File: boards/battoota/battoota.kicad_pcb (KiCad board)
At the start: 2 copper layers, 122.6 x 88.9 mm, 23 parts

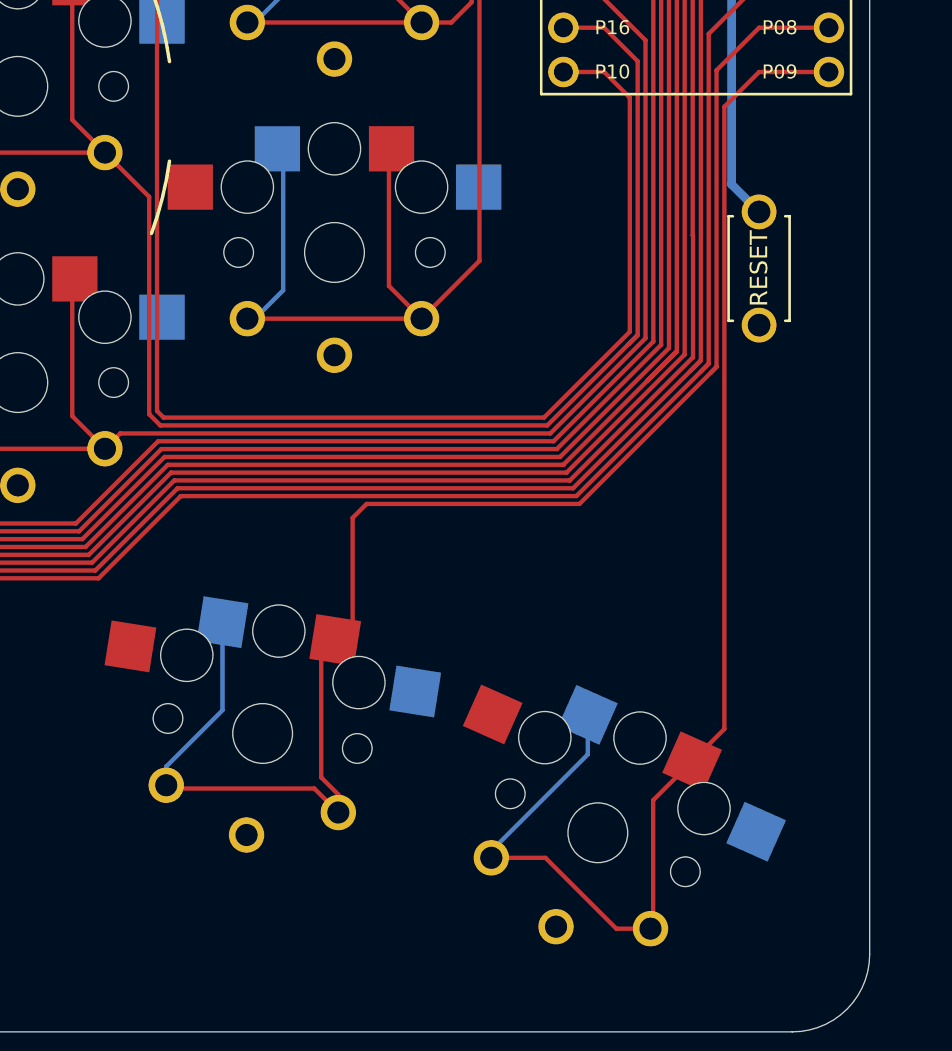
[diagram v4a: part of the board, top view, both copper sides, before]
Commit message: battoota thumb to original place
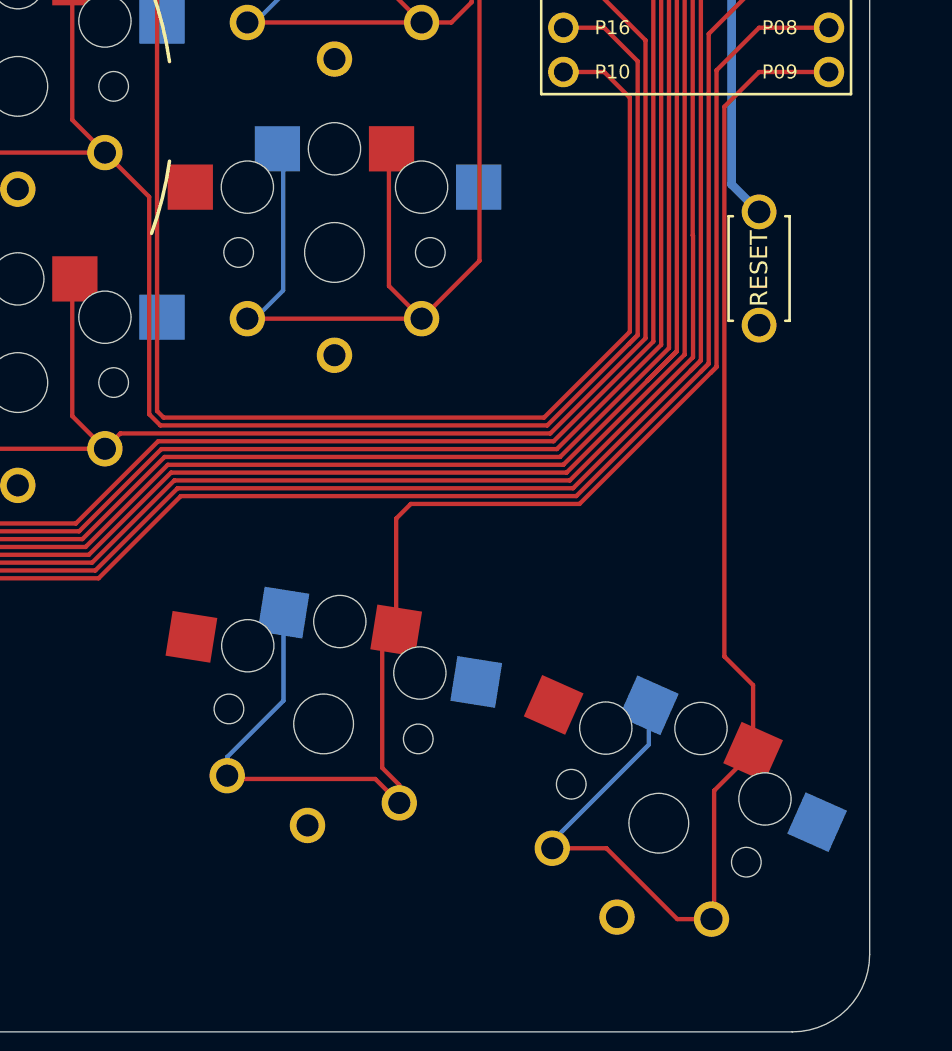
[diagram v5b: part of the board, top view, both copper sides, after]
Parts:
- moved S33 3.54 mm to (152.2, -45.8)
- moved S31 3.54 mm to (133.0, -51.5)
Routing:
- net P8: track 88.3 -> 84.1 mm
- net P9: track 77.1 -> 76.4 mm
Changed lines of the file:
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@@
   )
   (footprint "Alaa:choc_hotswap_key" (layer "F.Cu")
-    (at 148.714791 -45.238254 -24)
+    (at 152.214001 -45.787044 -24)
     (attr through_hole)
     (fp_text reference "S33" (at 0 0 139) (layer "F.SilkS") hide
@@
   )
   (footprint "Alaa:choc_hotswap_key" (layer "F.Cu")
-    (at 129.476118 -50.937009 -9)
+    (at 132.975328 -51.485799 -9)
     (attr through_hole)
     (fp_text reference "S31" (at 0 0 154) (layer "F.SilkS") hide
@@
   (segment (start 155.527414 -71.97371) (end 155.191874 -71.638171) (width 0.25) (layer "F.Cu") (net 16))
   (segment (start 161.977213 -91.442348) (end 157.969791 -91.442348) (width 0.25) (layer "F.Cu") (net 16))
-  (segment (start 135.441288 -64.111751) (end 134.641581 -63.312044) (width 0.25) (layer "F.Cu") (net 16))
-  (segment (start 133.820109 -47.432936) (end 133.820109 -46.401621) (width 0.25) (layer "F.Cu") (net 16))
-  (segment (start 132.839791 -48.413254) (end 133.820109 -47.432936) (width 0.25) (layer "F.Cu") (net 16))
-  (segment (start 124.130937 -47.778254) (end 123.943226 -47.965965) (width 0.25) (layer "F.Cu") (net 16))
+  (segment (start 147.665453 -64.111751) (end 137.981288 -64.111751) (width 0.25) (layer "F.Cu") (net 16))
+  (segment (start 137.319319 -47.981726) (end 137.319319 -46.950411) (width 0.25) (layer "F.Cu") (net 16))
+  (segment (start 136.339001 -48.962044) (end 137.319319 -47.981726) (width 0.25) (layer "F.Cu") (net 16))
+  (segment (start 127.630147 -48.327044) (end 127.442436 -48.514755) (width 0.25) (layer "F.Cu") (net 16))
+  (segment (start 137.140791 -63.271254) (end 137.140791 -56.850221) (width 0.25) (layer "F.Cu") (net 16))
+  (segment (start 155.527414 -71.973711) (end 155.191874 -71.638171) (width 0.25) (layer "F.Cu") (net 16))
+  (segment (start 155.527414 -88.999971) (end 155.527414 -71.973711) (width 0.25) (layer "F.Cu") (net 16))
+  (segment (start 137.319319 -46.950411) (end 135.942686 -48.327044) (width 0.25) (layer "F.Cu") (net 16))
+  (segment (start 135.942686 -48.327044) (end 127.630147 -48.327044) (width 0.25) (layer "F.Cu") (net 16))
+  (segment (start 137.981288 -64.111751) (end 137.140791 -63.271254) (width 0.25) (layer "F.Cu") (net 16))
+  (segment (start 136.339001 -56.048429) (end 136.339001 -48.962044) (width 0.25) (layer "F.Cu") (net 16))
   (segment (start 155.191874 -71.638171) (end 147.665453 -64.111751) (width 0.25) (layer "F.Cu") (net 16))
-  (segment (start 155.527414 -71.973711) (end 155.191874 -71.638171) (width 0.25) (layer "F.Cu") (net 16))
-  (segment (start 134.641581 -63.312044) (end 134.641581 -56.301431) (width 0.25) (layer "F.Cu") (net 16))
-  (segment (start 155.527414 -88.999971) (end 155.527414 -71.973711) (width 0.25) (layer "F.Cu") (net 16))
-  (segment (start 133.820109 -46.401621) (end 132.443476 -47.778254) (width 0.25) (layer "F.Cu") (net 16))
-  (segment (start 132.443476 -47.778254) (end 124.130937 -47.778254) (width 0.25) (layer "F.Cu") (net 16))
-  (segment (start 134.641583 -56.301431) (end 133.839791 -55.499639) (width 0.25) (layer "F.Cu") (net 16))
-  (segment (start 147.665453 -64.111751) (end 135.441288 -64.111751) (width 0.25) (layer "F.Cu") (net 16))
-  (segment (start 132.839791 -55.499639) (end 132.839791 -48.413254) (width 0.25) (layer "F.Cu") (net 16))
   (segment (start 157.969791 -91.442348) (end 155.527414 -88.999971) (width 0.25) (layer "F.Cu") (net 16))
-  (segment (start 123.943226 -49.041689) (end 123.943226 -47.965965) (width 0.25) (layer "B.Cu") (net 16))
-  (segment (start 127.172224 -52.270687) (end 123.943226 -49.041689) (width 0.25) (layer "B.Cu") (net 16))
-  (segment (start 127.172224 -57.326077) (end 127.172224 -52.270687) (width 0.25) (layer "B.Cu") (net 16))
-  (segment (start 151.889791 -39.88597) (end 151.736919 -39.733098) (width 0.25) (layer "F.Cu") (net 17))
+  (segment (start 127.442435 -49.590478) (end 127.442435 -48.514756) (width 0.25) (layer "B.Cu") (net 16))
+  (segment (start 130.671434 -57.874867) (end 130.671434 -52.819477) (width 0.25) (layer "B.Cu") (net 16))
+  (segment (start 130.671434 -52.819477) (end 127.442435 -49.590478) (width 0.25) (layer "B.Cu") (net 16))
+  (segment (start 155.976934 -55.359111) (end 157.625944 -53.710101) (width 0.25) (layer "F.Cu") (net 17))
+  (segment (start 155.389001 -40.43476) (end 155.236129 -40.281888) (width 0.25) (layer "F.Cu") (net 17))
   (segment (start 161.977213 -88.902348) (end 157.969791 -88.902348) (width 0.25) (layer "F.Cu") (net 17))
-  (segment (start 151.889791 -47.104843) (end 151.889791 -39.88597) (width 0.25) (layer "F.Cu") (net 17))
-  (segment (start 149.774947 -39.733098) (end 145.707581 -43.800464) (width 0.25) (layer "F.Cu") (net 17))
-  (segment (start 155.976934 -51.191986) (end 154.126734 -49.341786) (width 0.25) (layer "F.Cu") (net 17))
-  (segment (start 151.736919 -39.733098) (end 149.774947 -39.733098) (width 0.25) (layer "F.Cu") (net 17))
-  (segment (start 145.707581 -43.800464) (end 142.601465 -43.800464) (width 0.25) (layer "F.Cu") (net 17))
   (segment (start 157.969791 -88.902348) (end 155.976934 -86.909491) (width 0.25) (layer "F.Cu") (net 17))
-  (segment (start 154.126735 -49.341787) (end 151.889791 -47.104843) (width 0.25) (layer "F.Cu") (net 17))
-  (segment (start 155.976934 -86.909491) (end 155.976934 -51.191986) (width 0.25) (layer "F.Cu") (net 17))
-  (segment (start 148.143013 -52.005911) (end 148.143013 -49.746476) (width 0.25) (layer "B.Cu") (net 17))
-  (segment (start 148.143013 -49.746476) (end 142.601465 -44.204928) (width 0.25) (layer "B.Cu") (net 17))
-  (segment (start 142.601465 -44.204928) (end 142.601465 -43.800464) (width 0.25) (layer "B.Cu") (net 17))
+  (segment (start 155.389001 -47.653633) (end 155.389001 -40.43476) (width 0.25) (layer "F.Cu") (net 17))
+  (segment (start 157.625944 -53.710101) (end 157.625944 -49.890576) (width 0.25) (layer "F.Cu") (net 17))
+  (segment (start 153.274157 -40.281888) (end 149.206791 -44.349254) (width 0.25) (layer "F.Cu") (net 17))
+  (segment (start 155.236129 -40.281888) (end 153.274157 -40.281888) (width 0.25) (layer "F.Cu") (net 17))
+  (segment (start 149.206791 -44.349254) (end 146.100675 -44.349254) (width 0.25) (layer "F.Cu") (net 17))
+  (segment (start 155.976934 -86.909491) (end 155.976934 -55.359111) (width 0.25) (layer "F.Cu") (net 17))
+  (segment (start 157.625945 -49.890577) (end 155.389001 -47.653633) (width 0.25) (layer "F.Cu") (net 17))
+  (segment (start 151.642223 -52.554701) (end 151.642223 -50.295266) (width 0.25) (layer "B.Cu") (net 17))
+  (segment (start 151.642223 -50.295266) (end 146.100675 -44.753718) (width 0.25) (layer "B.Cu") (net 17))
+  (segment (start 146.100675 -44.753718) (end 146.100675 -44.349254) (width 0.25) (layer "B.Cu") (net 17))
   (segment (start 152.372041 -116.88499) (end 150.419502 -116.88499) (width 0.5) (layer "F.Cu") (net 18))
   (segment (start 136.618406 -117.166566) (end 137.420433 -116.364539) (width 0.5) (layer "F.Cu") (net 18))
